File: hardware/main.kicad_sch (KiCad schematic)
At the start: 506 parts, among them J1 TYPE-C-31-M-12, J3 USB_C_Receptacle, J5 DS1128-09-S8B8X, Q1 SSM6J501NU, Q2 SSM6J501NU, Q3 FDV301N, Q4 BC817, SW1 TS-1187A-B-A-B, SW2 TS-1187A-B-A-B, SW3 TS-1187A-B-A-B, U1 SN74LVC1G175, U2 IP5328P, U3 MT3420B, U4 MT3420B, U5 TPS63020, U6 TPS63020, U7 MT3420B, U8 MT3420B

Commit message: init pcb
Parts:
- removed BT1, BT2, BT3, BT4: BH-18650-B1BA002, MAS_Package_nostd:BatteryHolder_BH-18650-B1BA002, symbol Device:Battery_Cell
- removed C1, C16, C17, C18, C19, C23, C24, C25, C27, C30, C31, C34, C35, C4, C5, C55, C56, C? (x6): 10u, Capacitor_SMD:C_0805_2012Metric, symbol Device:C_Small
- removed C10, C11, C12, C2, C20, C21, C32, C33, C36, C37, C38, C39, C42, C43, C44, C50, C51, C6, C7, C9, C? (x88): 100n, Capacitor_SMD:C_0603_1608Metric, symbol Device:C_Small
- removed C13, C22, C26, C?: 22u, Capacitor_SMD:C_0805_2012Metric, symbol Device:C_Small
- removed C14, C15, C45, C46: 22p, Capacitor_SMD:C_0603_1608Metric, symbol Device:C_Small
- removed C28, C29, C3, C47, C48, C49, C52, C8, C? (x2): 2.2u, Capacitor_SMD:C_0805_2012Metric, symbol Device:C_Small
- removed C40, C41: 4.7p, Capacitor_SMD:C_0603_1608Metric, symbol Device:C_Small
- removed C53: 100u, Capacitor_Tantalum_SMD:CP_EIA-7343-31_Kemet-D, symbol Device:C_Polarized_Small
- removed C54: 100uF, Capacitor_Tantalum_SMD:CP_EIA-3528-21_Kemet-B, symbol main-rescue:CP_Small-Device
- removed C? (x10): 1u, Capacitor_SMD:C_0805_2012Metric, symbol Device:C_Small
- removed C? (x4): 1.2p, Capacitor_SMD:C_0603_1608Metric, symbol Device:C_Small
- removed C? (x4): 470n, Capacitor_SMD:C_0603_1608Metric, symbol Device:C_Small
- removed C? (x2): 9p, Capacitor_SMD:C_0603_1608Metric, symbol Device:C_Small
- removed C? (x4): 0.5p, Capacitor_SMD:C_0603_1608Metric, symbol Device:C_Small
- removed C? (x9): 4.7u, Capacitor_SMD:C_0805_2012Metric, symbol Device:C_Small
- removed C? (x4): 10p, Capacitor_SMD:C_0603_1608Metric, symbol Device:C_Small
- removed C? (x2): 18p, Capacitor_SMD:C_0603_1608Metric, symbol Device:C_Small
- removed C? (x4): 3p, Capacitor_SMD:C_0603_1608Metric, symbol Device:C_Small
- removed C? (x4): ~, Capacitor_SMD:C_0603_1608Metric, symbol Device:C_Small
- removed C? (x3): 1n, Capacitor_SMD:C_0805_2012Metric, symbol Device:C_Small
- removed D1: LEDY, Diode_SMD:D_0603_1608Metric, symbol Device:LED_Small
- removed D2: LEDG, Diode_SMD:D_0603_1608Metric, symbol Device:LED_Small
- removed D3: MBR0540, Diode_SMD:D_SOD-123, symbol Diode:MBR0540
- removed F1, F2, F3, F4: 0466001.NRHF, MAS_Package_std:Fuse_1812_4532Metric, symbol Device:Fuse_Small
- removed J1: TYPE-C-31-M-12, MAS_Package_std:USB_C_Receptacle_HRO_TYPE-C-31-M-12, symbol Connector:USB_C_Receptacle_USB2.0
- removed J3: USB_C_Receptacle, symbol Connector:USB_C_Receptacle
- removed J5, J? (x2): DS1128-09-S8B8X, MAS_Package_std:RJ45_DS1128-09-S8B8X, symbol MAS_Connectors:DS1128-09-S8B8X
- removed J? (x2): IDC-08M, Connector_PinHeader_1.27mm:PinHeader_2x04_P1.27mm_Vertical, symbol Connector_Generic:Conn_02x04_Counter_Clockwise
- removed J? (x2): SMA-KWE901, MAS_Package_std:SMA_Amphenol_901-143_Horizontal, symbol Connector:Conn_Coaxial
- removed JP1, JP2, JP3, JP4, JP5, JP6, JP7: J_Boot, Jumper:SolderJumper-2_P1.3mm_Open_Pad1.0x1.5mm, symbol Jumper:Jumper_2_Open
- removed L1, L2, L3, L4, L6, L7, L?: SLO0530H2R2MTT, MAS_Package_std:Power_inductor_SMD_0530, symbol pspice:INDUCTOR
- removed L5: SLO0530H1R0MTT, MAS_Package_std:Power_inductor_SMD_0530, symbol pspice:INDUCTOR
- removed L? (x4): VHF160808H1N8ST, Inductor_SMD:L_0603_1608Metric, symbol pspice:INDUCTOR
- removed L? (x4): HK16082N7S-T, Inductor_SMD:L_0603_1608Metric, symbol pspice:INDUCTOR
- removed L? (x4): SDCL1608C3N0STDF, Inductor_SMD:L_0603_1608Metric, symbol pspice:INDUCTOR
- removed L? (x2): CBM160808U121T, Inductor_SMD:L_0603_1608Metric, symbol pspice:INDUCTOR
- removed L? (x2): ~, Inductor_SMD:L_0603_1608Metric, symbol pspice:INDUCTOR
- removed L? (x2): SDCL1608C1N2STDF, Inductor_SMD:L_0603_1608Metric, symbol pspice:INDUCTOR
- removed Q1, Q2: SSM6J501NU, MAS_Package_std:U-MOSVI, symbol MAS_Transistors:SSM6J501NU
- removed Q3: FDV301N, Package_TO_SOT_SMD:SOT-23, symbol MAS_Transistors:FDV301N
- removed Q4: BC817, Package_TO_SOT_SMD:SOT-23, symbol Transistor_BJT:BC817
- removed R1: 2k, Resistor_SMD:R_0603_1608Metric, symbol Device:R_Small
- removed R10, R16, R18, R25, R26, R27, R34, R36, R37, R39, R6, R7: 100k, Resistor_SMD:R_0603_1608Metric, symbol Device:R_Small
- removed R11: 100k (NTC), Resistor_SMD:R_0805_2012Metric, symbol MAS_Resistors:Thermistor_NTC
- removed R12, R21, R22, R23, R24, R3, R40, R? (x9): 1k, Resistor_SMD:R_0603_1608Metric, symbol Device:R_Small
- removed R13, R? (x34): ~, Resistor_SMD:R_0603_1608Metric, symbol Device:R_Small
- removed R14, R15, R? (x27): 4.7k, Resistor_SMD:R_0603_1608Metric, symbol Device:R_Small
- removed R17: 120k, Resistor_SMD:R_0603_1608Metric, symbol Device:R_Small
- removed R19, R38: 150k, Resistor_SMD:R_0603_1608Metric, symbol Device:R_Small
- removed R2, R28, R4, R? (x2): 10k, Resistor_SMD:R_0603_1608Metric, symbol Device:R_Small
- removed R20, R35, R5: 470R, Resistor_SMD:R_0805_2012Metric, symbol Device:R_Small
- removed R29: 1.1k, Resistor_SMD:R_0603_1608Metric, symbol Device:R_Small
- removed R30: 330k, Resistor_SMD:R_0603_1608Metric, symbol Device:R_Small
- removed R31: 51k, Resistor_SMD:R_0603_1608Metric, symbol Device:R_Small
- removed R32, R33: 68k, Resistor_SMD:R_0603_1608Metric, symbol Device:R_Small
- removed R8: 0.01R, Resistor_SMD:R_1206_3216Metric, symbol Device:R_Small
- removed R9: 82k, Resistor_SMD:R_0603_1608Metric, symbol Device:R_Small
- removed R? (x21): 0R, Resistor_SMD:R_0603_1608Metric, symbol Device:R_Small
- removed R? (x7): 22R, Resistor_SMD:R_0603_1608Metric, symbol Device:R_Small
- removed R? (x2): 240R, Resistor_SMD:R_0603_1608Metric, symbol Device:R_Small
- removed R?: 910k, Resistor_SMD:R_0603_1608Metric, symbol Device:R_Small
- removed R? (x12): 75R, Resistor_SMD:R_0603_1608Metric, symbol Device:R_Small
- removed R? (x2): 22k, Resistor_SMD:R_0603_1608Metric, symbol Device:R_Small
- removed R?: 5.1k, Resistor_SMD:R_0603_1608Metric, symbol Device:R_Small
- removed R? (x6): 330R, Resistor_SMD:R_0805_2012Metric, symbol Device:R_Small
- removed R? (x4): 51R, Resistor_SMD:R_0603_1608Metric, symbol Device:R_Small
- removed R? (x3): 24k, Resistor_SMD:R_0603_1608Metric, symbol Device:R_Small
- removed R?: 100R, Resistor_SMD:R_0603_1608Metric, symbol Device:R_Small
- removed RN?: 4D03WGJ0102T5E, Resistor_SMD:R_Array_Convex_4x0603, symbol Device:R_Pack04
- removed SW1, SW2, SW3, SW?: TS-1187A-B-A-B, Button_Switch_SMD:SW_SPST_TL3342, symbol Switch:SW_Push
- removed TP1, TP2, TP3, TP4, TP? (x30): TestPoint, TestPoint:TestPoint_Pad_D1.0mm, symbol Connector:TestPoint
- removed TR? (x3): H2450G, MAS_Package_nostd:Transformer_Ethernet_E-NETTR_24, symbol MAS_Transformers:H2450G
- removed U1: SN74LVC1G175, Package_TO_SOT_SMD:SOT-23-6, symbol MAS_IC_Logic:SN74LVC1G175
- removed U2: IP5328P, Package_DFN_QFN:QFN-40-1EP_6x6mm_P0.5mm_EP4.6x4.6mm, symbol MAS_IC_PowerSupply:IP5328P
- removed U3, U4, U7, U8: MT3420B, Package_TO_SOT_SMD:SOT-23-6, symbol MAS_IC_PowerSupply:MT3420
- removed U5, U6: TPS63020, Package_DFN_QFN:DFN-14-1EP_3x4mm_P0.5mm_EP1.7x3.3mm, symbol MAS_IC_PowerSupply:TPS6302x
- removed U? (x5): MT7621A, MAS_Package_std:TFBGA-387_11.7x13.6mm_P0.65mm, symbol MAS_IC_MCU:MT7621A
- removed U?: W25Q256FVEIG, MAS_Package_std:WSON-8-1EP_8x6mm_P1.27mm_EP3.4x4mm, symbol MAS_IC_Memory:W25Qx
- removed U?: NT5CB64M16FP-DH (!), Package_BGA:BGA-96_9.0x13.0mm_Layout2x3x16_P0.8mm, symbol Memory_RAM:AS4C256M16D3
- removed U?: N096-2864KSWEG01-H30, MAS_Package_nostd:SSD1306-oled-0.96, symbol MAS_Module:SSD1306-OLED-0.96
- removed U? (x3): TPD2EUSB30, Package_TO_SOT_SMD:Texas_DRT-3, symbol Power_Protection:TPD2EUSB30
- removed U?: MT7603E, MAS_Package_std:QFN-56-1EP_7x7mm_P0.4mm_EP4.6x4.6mm, symbol MAS_RF:MT7603E
- removed X?: HSO321S-50MHZ-3.3V, MAS_Package_std:Oscillator_SMD_SMD3225-4P, symbol Oscillator:ASV-xxxMHz
- removed Y?: X322540MPB4SI, MAS_Package_std:Oscillator_SMD_SMD3225-4P, symbol Device:Crystal_GND24
- gave numbers to parts that had none: 1
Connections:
- no-connect marks 45 -> 0
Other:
- added sheet Charger (charger.kicad_sch)
- added sheet Ethernet (ethernet.kicad_sch)
- added sheet Interface (interface.kicad_sch)
- added sheet Memory (memory.kicad_sch)
- added sheet Other (other.kicad_sch)
- added sheet Power (power.kicad_sch)
- added sheet RF (rf.kicad_sch)
- note removed: "!!!"
- note removed: "SPI_CLK"
- note removed: "SPI_CS0_N"
- note removed: "SPI_CS1_N"
- moved on the sheet: FID1, FID2, FID3, FID4, FID5, FID6, H1, H2, H3, H4

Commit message: update cap and dru
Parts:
- added F1, F2: 12T.30000063AG12S1B02, Fuse:Fuse_1206_3216Metric, symbol Device:Fuse_Small
- added J4: 98424-G52-04ALF, MAS_Package_std:PinSocket_2x02_P2.00mm_Vertical_SMD, symbol Connector_Generic:Conn_02x02_Top_Bottom
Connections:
- new net: F1.1, J4.3 (Pin_3)
- new net: F2.1, J4.4 (Pin_4)
- new net +BATT: F1.2, F2.2
- new net -BATT: J4.1 (Pin_1), J4.2 (Pin_2)
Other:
- removed sheet RF

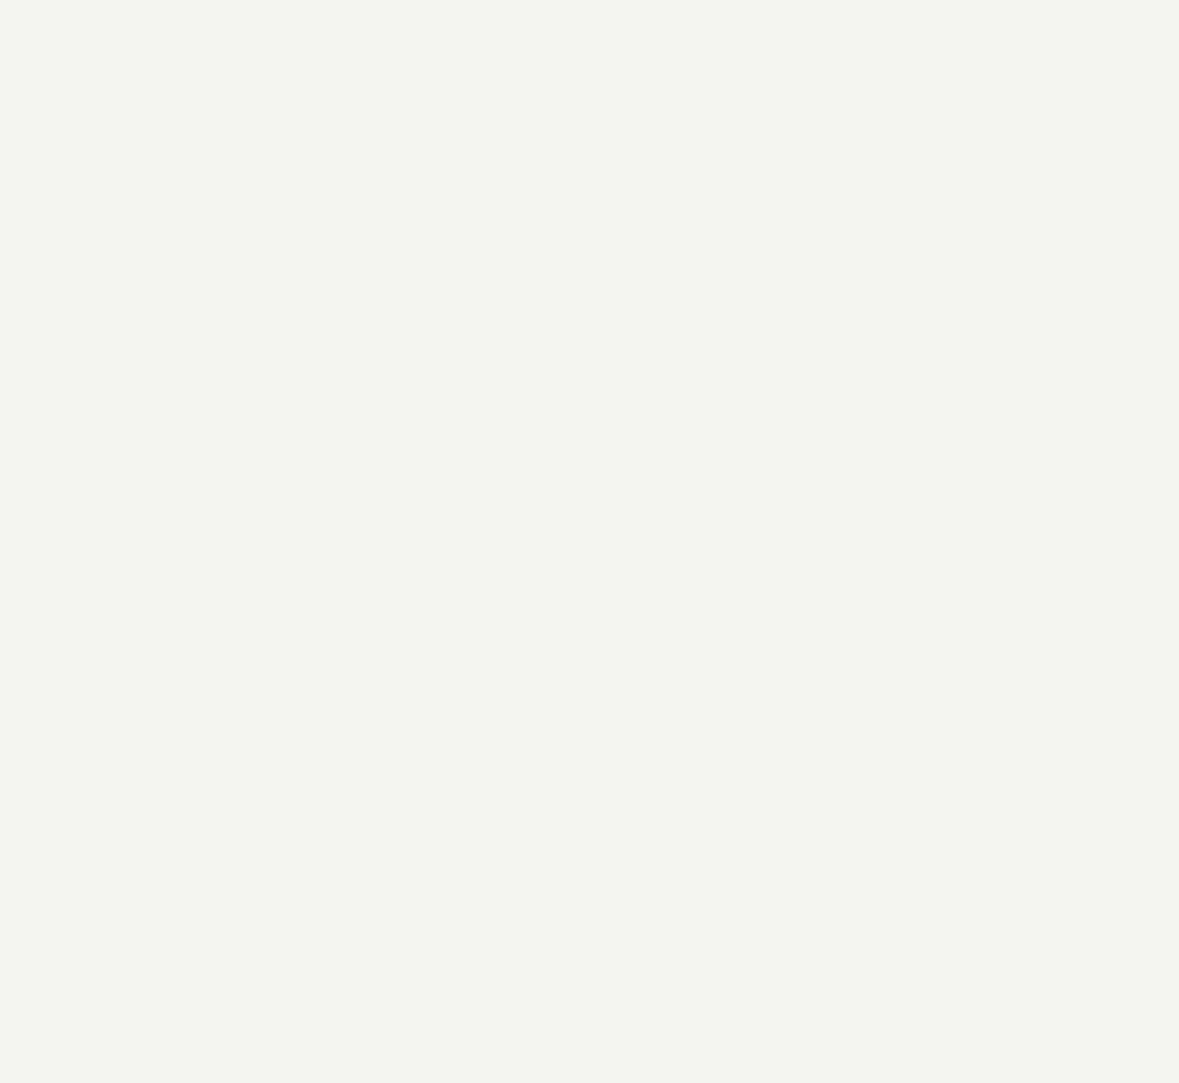
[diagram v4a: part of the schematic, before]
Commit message: add mini-pcie and m2
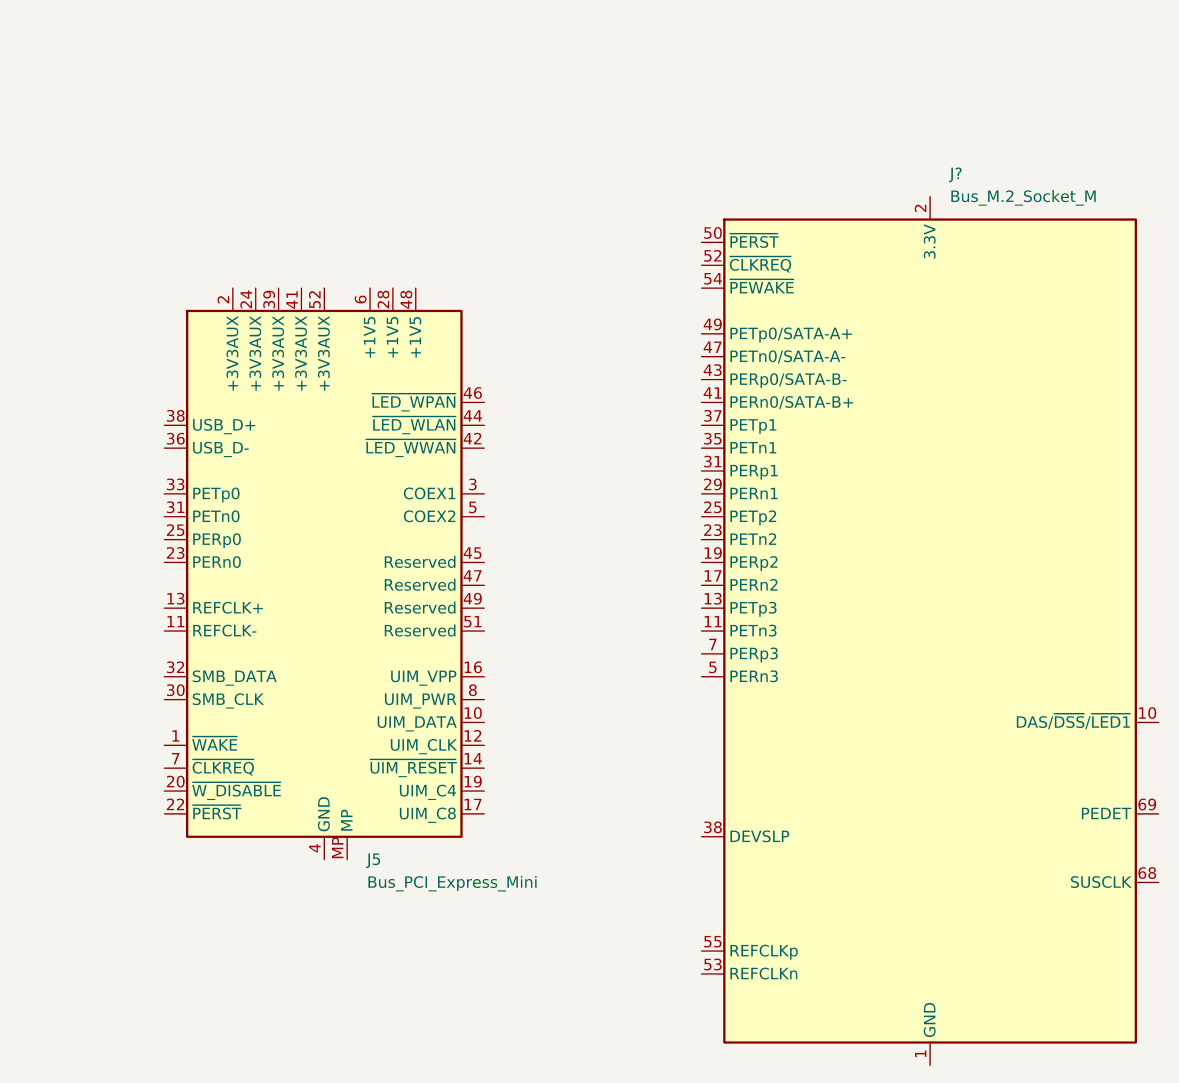
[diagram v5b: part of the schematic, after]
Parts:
- added J5: Bus_PCI_Express_Mini, Connector_PCBEdge:BUS_PCI_Express_Mini_Dual, symbol Connector:Bus_PCI_Express_Mini
- added J?: Bus_M.2_Socket_M, symbol Connector:Bus_M.2_Socket_M
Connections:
- new net: J?.1 (GND), J?.15 (GND), J?.21 (GND), J?.27 (GND), J?.3 (GND), J?.33 (GND), J?.39 (GND), J?.45 (GND), J?.51 (GND), J?.57 (GND), J?.71 (GND), J?.73 (GND), J?.75 (GND), J?.9 (GND)
- new net: J?.12 (3.3V), J?.14 (3.3V), J?.16 (3.3V), J?.18 (3.3V), J?.2 (3.3V), J?.4 (3.3V), J?.70 (3.3V), J?.72 (3.3V), J?.74 (3.3V)
- new net: J5.15 (GND), J5.18 (GND), J5.21 (GND), J5.26 (GND), J5.27 (GND), J5.29 (GND), J5.34 (GND), J5.35 (GND), J5.37 (GND), J5.4 (GND), J5.40 (GND), J5.43 (GND), J5.50 (GND), J5.9 (GND)
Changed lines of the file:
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@@
+    )
+  )
+  (symbol (lib_id "Connector:Bus_M.2_Socket_M") (at 320.04 102.87 0) (unit 1)
+    (in_bom yes) (on_board yes) (dnp no) (fields_autoplaced)
+    (property "Reference" "J?" (at 322.2341 52.07 0)
+      (effects (font (size 1.27 1.27)) (justify left))
+    )
+    (property "Value" "Bus_M.2_Socket_M" (at 322.2341 54.61 0)
+      (effects (font (size 1.27 1.27)) (justify left))
+    )
+    (property "Footprint" "" (at 320.04 76.2 0)
+      (effects (font (size 1.27 1.27)) hide)
+    )
+    (property "Datasheet" "http://read.pudn.com/downloads794/doc/project/3133918/PCIe_M.2_Electromechanical_Spec_Rev1.0_Final_11012013_RS_Clean.pdf#page=155" (at 320.04 76.2 0)
+      (effects (font (size 1.27 1.27)) hide)
+    )
+    (pin "1")
+    (pin "10")
+    (pin "11")
+    (pin "12")
+    (pin "13")
+    (pin "14")
+    (pin "15")
+    (pin "16")
+    (pin "17")
+    (pin "18")
+    (pin "19")
+    (pin "2")
+    (pin "20")
+    (pin "21")
+    (pin "22")
+    (pin "23")
+    (pin "24")
+    (pin "25")
+    (pin "26")
+    (pin "27")
+    (pin "28")
+    (pin "29")
+    (pin "3")
+    (pin "30")
+    (pin "31")
+    (pin "32")
+    (pin "33")
+    (pin "34")
+    (pin "35")
+    (pin "36")
+    (pin "37")
+    (pin "38")
+    (pin "39")
+    (pin "4")
+    (pin "40")
+    (pin "41")
+    (pin "42")
+    (pin "43")
+    (pin "44")
+    (pin "45")
+    (pin "46")
+    (pin "47")
+    (pin "48")
+    (pin "49")
+    (pin "5")
+    (pin "50")
+    (pin "51")
+    (pin "52")
+    (pin "53")
+    (pin "54")
+    (pin "55")
+    (pin "56")
+    (pin "57")
+    (pin "58")
+    (pin "6")
+    (pin "67")
+    (pin "68")
+    (pin "69")
+    (pin "7")
+    (pin "70")
+    (pin "71")
+    (pin "72")
+    (pin "73")
+    (pin "74")
+    (pin "75")
+    (pin "8")
+    (pin "9")
+    (instances
+      (project "main"
+        (path "/c6e5d5ba-43a3-4ff8-a766-3efdb024d1f4"
+          (reference "J?") (unit 1)
+        )
+      )
     )
   )
@@
         )
       )
+    )
+  )
+  (symbol (lib_id "Connector:Bus_PCI_Express_Mini") (at 252.73 97.79 0) (unit 1)
+    (in_bom yes) (on_board yes) (dnp no) (fields_autoplaced)
+    (property "Reference" "J5" (at 257.4641 128.27 0)
+      (effects (font (size 1.27 1.27)) (justify left))
+    )
+    (property "Value" "Bus_PCI_Express_Mini" (at 257.4641 130.81 0)
+      (effects (font (size 1.27 1.27)) (justify left))
+    )
+    (property "Footprint" "Connector_PCBEdge:BUS_PCI_Express_Mini_Dual" (at 252.73 97.79 0)
+      (effects (font (size 1.27 1.27)) hide)
+    )
+    (property "Datasheet" "~" (at 248.92 127 0)
+      (effects (font (size 1.27 1.27)) hide)
+    )
+    (pin "1")
+    (pin "10")
+    (pin "11")
+    (pin "12")
+    (pin "13")
+    (pin "14")
+    (pin "15")
+    (pin "16")
+    (pin "17")
+    (pin "18")
+    (pin "19")
+    (pin "2")
+    (pin "20")
+    (pin "21")
+    (pin "22")
+    (pin "23")
+    (pin "24")
+    (pin "25")
+    (pin "26")
+    (pin "27")
+    (pin "28")
+    (pin "29")
+    (pin "3")
+    (pin "30")
+    (pin "31")
+    (pin "32")
+    (pin "33")
+    (pin "34")
+    (pin "35")
+    (pin "36")
+    (pin "37")
+    (pin "38")
+    (pin "39")
+    (pin "4")
+    (pin "40")
+    (pin "41")
+    (pin "42")
+    (pin "43")
+    (pin "44")
+    (pin "45")
+    (pin "46")
+    (pin "47")
+    (pin "48")
+    (pin "49")
+    (pin "5")
+    (pin "50")
+    (pin "51")
+    (pin "52")
+    (pin "6")
+    (pin "7")
+    (pin "8")
+    (pin "9")
+    (pin "MP")
+    (instances
+      (project "main"
+        (path "/c6e5d5ba-43a3-4ff8-a766-3efdb024d1f4"
+          (reference "J5") (unit 1)
+        )
+      )

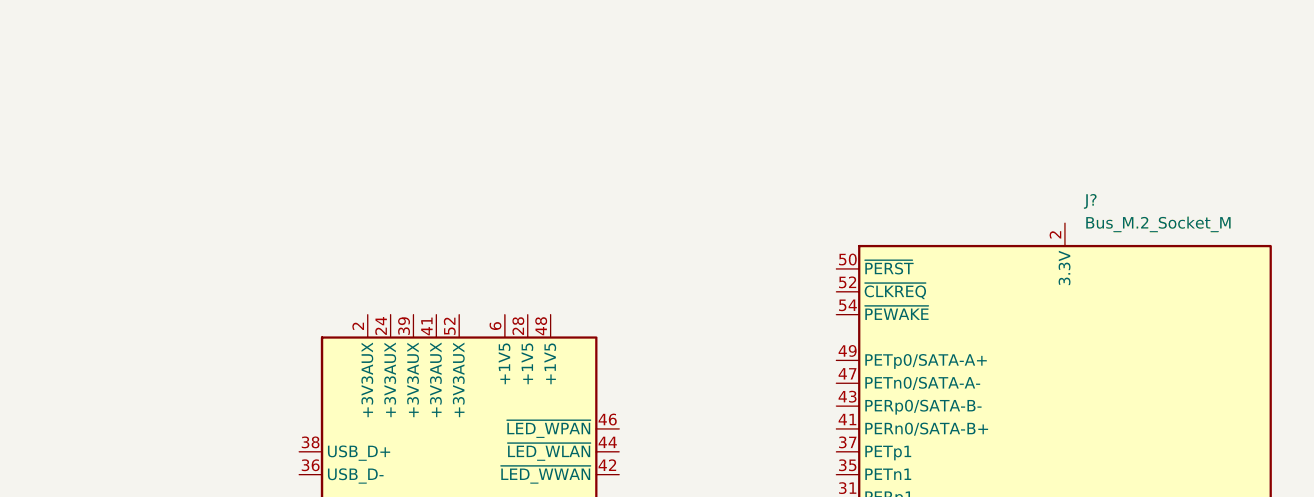
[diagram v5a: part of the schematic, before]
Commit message: add mPCI-e and m2 conn
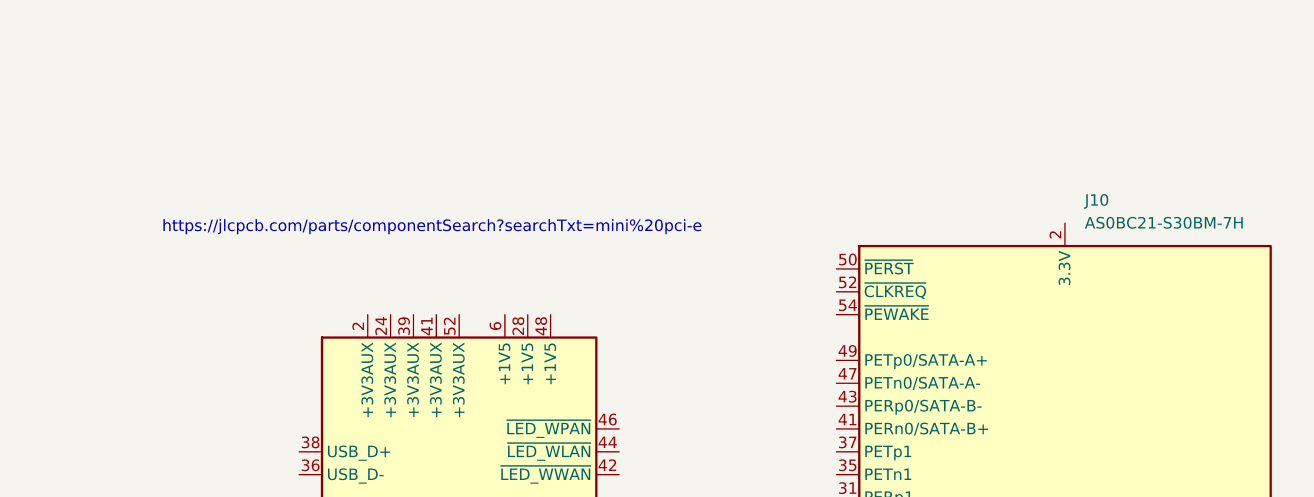
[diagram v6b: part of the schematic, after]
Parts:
- J10: renamed from J?; value Bus_M.2_Socket_M -> AS0BC21-S30BM-7H; footprint (none) -> MAS_Package_std:Bus_M.2_Socket_M; lcsc (none) -> C2832351
- J5: footprint Connector_PCBEdge:BUS_PCI_Express_Mini_Dual -> MAS_Package_std:BUS_PCI_Express_Mini_Dual
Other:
- note added: "https://jlcpcb.com/parts/componentSearch?searchTxt=mini%20pci-e"
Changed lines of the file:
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@@
     (stroke (width 0) (type default))
+  )
+  (text "https://jlcpcb.com/parts/componentSearch?searchTxt=mini%20pci-e"
+    (at 219.71 55.88 0)
+    (effects (font (size 1.27 1.27)) (justify left bottom))
   )
   (label "PCIE_CK1_P" (at 60.96 130.81 180) (fields_autoplaced)
@@
   (symbol (lib_id "Connector:Bus_M.2_Socket_M") (at 320.04 102.87 0) (unit 1)
     (in_bom yes) (on_board yes) (dnp no) (fields_autoplaced)
-    (property "Reference" "J?" (at 322.2341 52.07 0)
-      (effects (font (size 1.27 1.27)) (justify left))
-    )
-    (property "Value" "Bus_M.2_Socket_M" (at 322.2341 54.61 0)
-      (effects (font (size 1.27 1.27)) (justify left))
-    )
-    (property "Footprint" "" (at 320.04 76.2 0)
+    (property "Reference" "J10" (at 322.2341 52.07 0)
+      (effects (font (size 1.27 1.27)) (justify left))
+    )
+    (property "Value" "AS0BC21-S30BM-7H" (at 322.2341 54.61 0)
+      (effects (font (size 1.27 1.27)) (justify left))
+    )
+    (property "Footprint" "MAS_Package_std:Bus_M.2_Socket_M" (at 320.04 76.2 0)
       (effects (font (size 1.27 1.27)) hide)
     )
     (property "Datasheet" "http://read.pudn.com/downloads794/doc/project/3133918/PCIe_M.2_Electromechanical_Spec_Rev1.0_Final_11012013_RS_Clean.pdf#page=155" (at 320.04 76.2 0)
+      (effects (font (size 1.27 1.27)) hide)
+    )
+    (property "lcsc" "C2832351" (at 320.04 102.87 0)
       (effects (font (size 1.27 1.27)) hide)
     )
@@
       (project "main"
         (path "/c6e5d5ba-43a3-4ff8-a766-3efdb024d1f4"
-          (reference "J?") (unit 1)
+          (reference "J10") (unit 1)
         )
       )
@@
       (effects (font (size 1.27 1.27)) (justify left))
     )
-    (property "Footprint" "Connector_PCBEdge:BUS_PCI_Express_Mini_Dual" (at 252.73 97.79 0)
-      (effects (font (size 1.27 1.27)) hide)
-    )
+    (property "Footprint" "MAS_Package_std:BUS_PCI_Express_Mini_Dual" (at 252.73 97.79 0)
+      (effects (font (size 1.27 1.27)) hide)
+    )
